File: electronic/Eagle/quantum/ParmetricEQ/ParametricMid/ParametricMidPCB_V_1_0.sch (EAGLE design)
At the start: 83 parts, among them IC1 OP275_SOIC8, IC14 TL072, IC2 OP275_SOIC8, IC3 OP275_SOIC8, IC4 DAC084S085CIMM_NOPB, IC5 DAC084S085CIMM_NOPB, J1 90814-0204, J2 90814-0204, Q1 TRANSOSTOR_NPN, Q2 TRANSOSTOR_NPN, U1 THAT2181SO8-US, U2 THAT2181SO8-US, U3 THAT2181SO8-US

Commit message: updates ParametricEQ
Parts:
- removed C19: 100 nF, passive components:CAPACITOR_0603
- removed C64: 10 uF, passive components:CAPACITOR_1206
- removed J1, J2: 90814-0204, electro_mechanical:90814-0204
- removed R60, R61, R67: 10 k, passive components:RESISTOR_0603
- removed R68: 20 k, passive components:RESISTOR_0603
- removed U$1, U$2: TL072, OP-AMPS:TL072
- removed Z1: ZENER_DIODE_BZT, passive components:ZENER_DIODE_BZT
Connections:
- removed net 1V_DAC_UNBUFFERD: C19.1, C64.1, R61.2, R68.1, U$2G$1.+IN
- removed net 2V_DAC_REF: R67.1, R68.2, Z1.K
- removed net AGND: C19.2, C64.2, R60.1, Z1.A
- removed net L-IN: J2.3
- removed net L-OUT: J2.4
- removed net N$67: R60.2, R61.1, U$2G$2.+IN
- net 0,5V_DAC: no longer U$2G$2.-IN, U$2G$2.OUT
- net 1V_DAC: no longer U$2G$1.-IN, U$2G$1.OUT
- net GND: no longer J1.3, J1.4
- net MID1_R-IN: no longer J2.1
- net MID1_R-OUT: no longer J2.2
- net V+: no longer J1.1, R67.2
- net V-: no longer J1.2
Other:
- note removed: "DAC Ref Voltages"

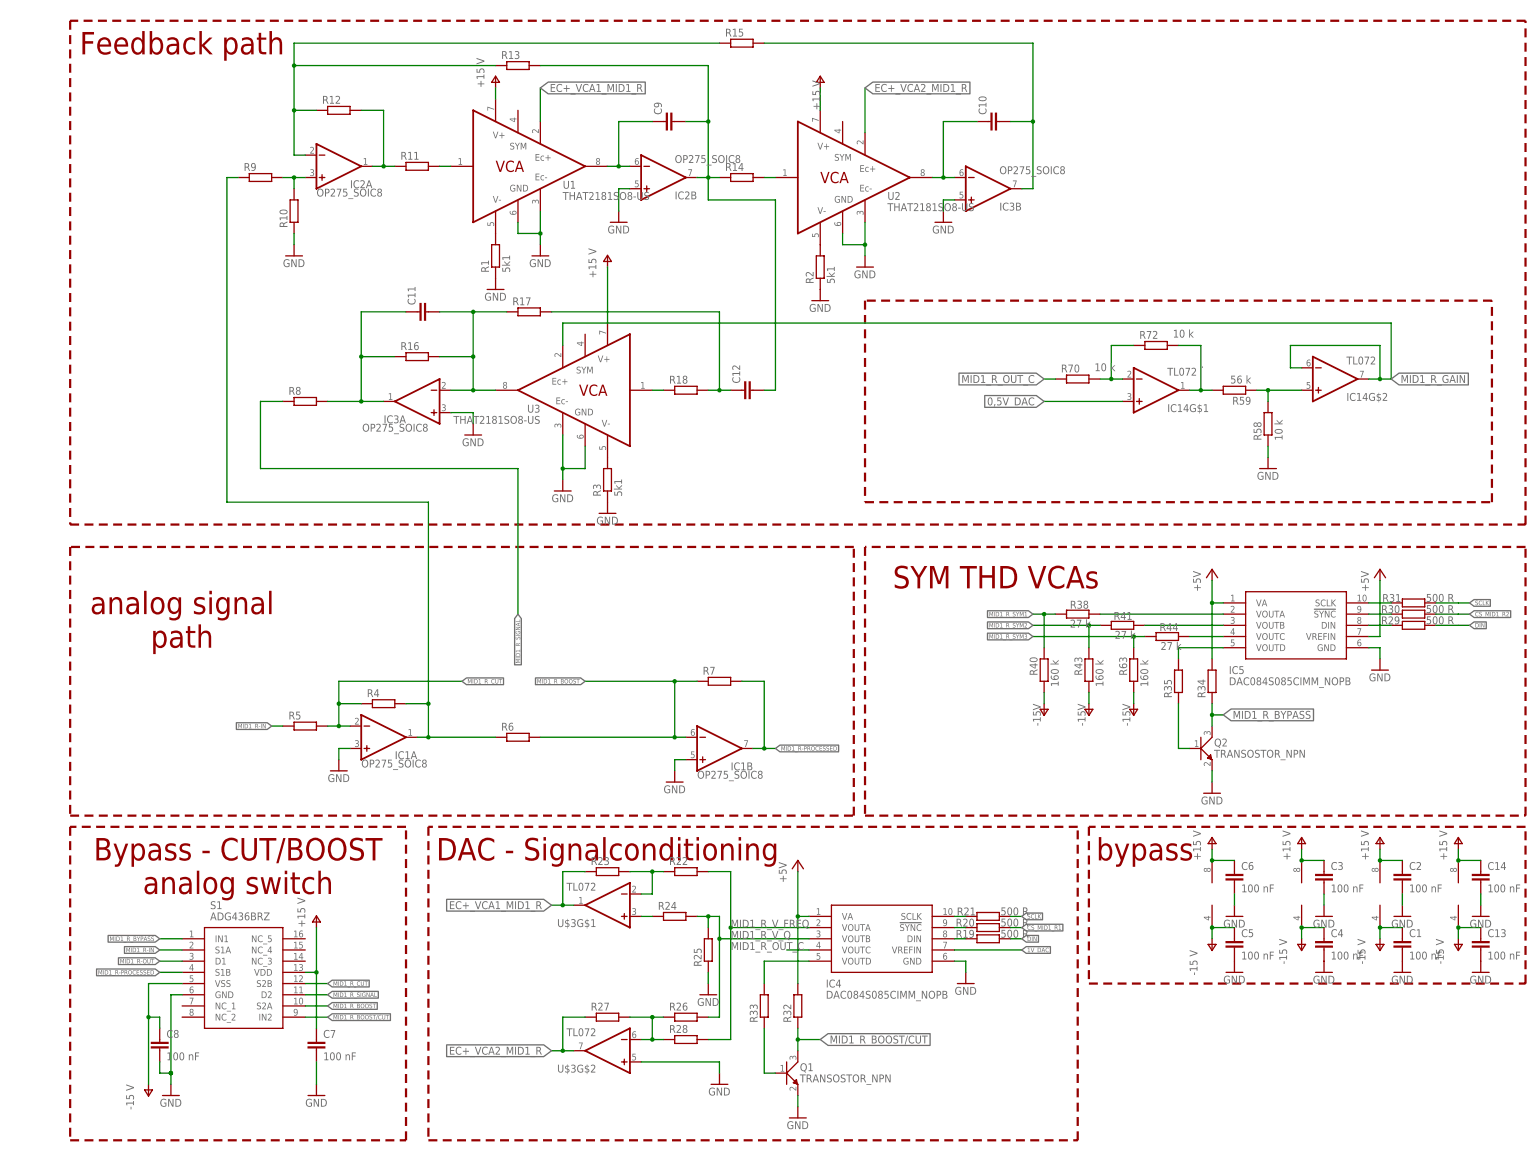
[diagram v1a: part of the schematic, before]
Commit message: split PCB in ParametricEQ
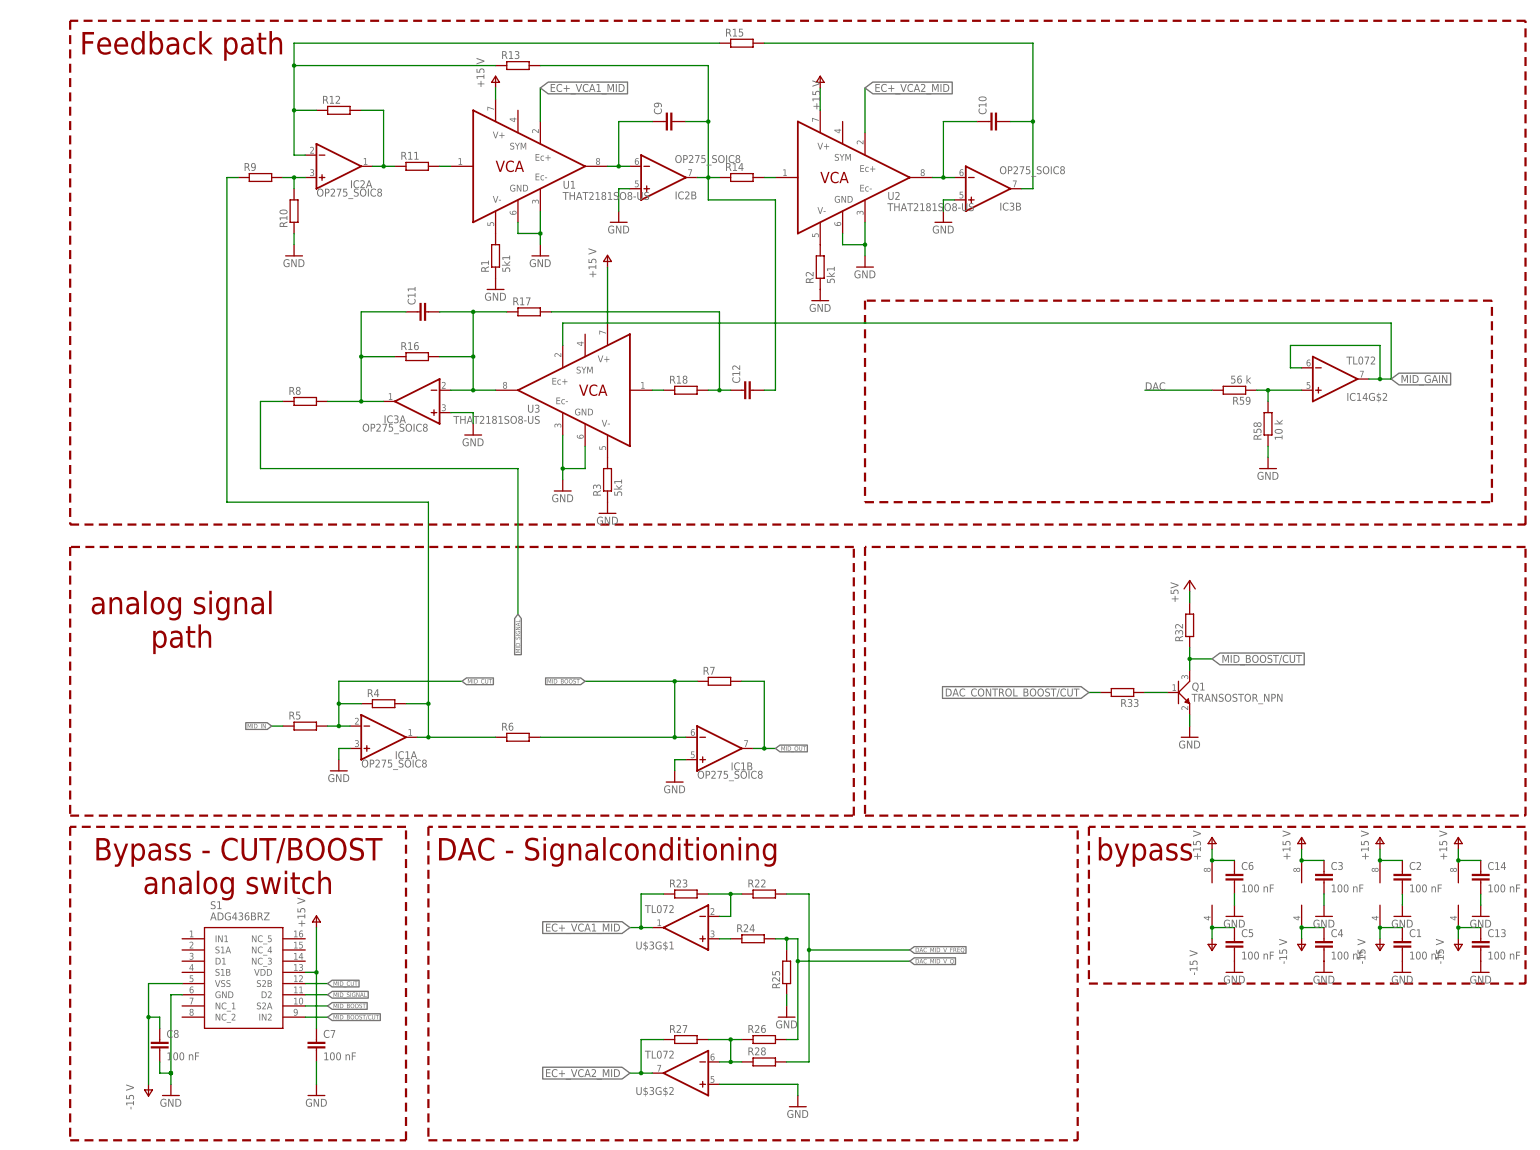
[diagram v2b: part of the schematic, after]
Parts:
- removed IC4, IC5: DAC084S085CIMM_NOPB, SPI:DAC084S085CIMM_NOPB
- removed Q2: TRANSOSTOR_NPN, active components:TRANSOSTOR_NPN
- removed R19, R20, R21, R29, R30, R31: 500 R, passive components:RESISTOR_0603
- removed R34, R35: (no value), passive components:RESISTOR_0603
- removed R38, R41, R44: 27 k, passive components:RESISTOR_0603
- removed R40, R43, R63: 160 k, passive components:RESISTOR_0603
- removed R70, R72: 10 k, passive components:RESISTOR_0603
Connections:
- net EC+_VCA1_MID1_R renamed EC+_VCA1_MID
- net EC+_VCA2_MID1_R renamed EC+_VCA2_MID
- net MID1_R_BOOST renamed MID_BOOST
- net MID1_R_BOOST/CUT renamed MID_BOOST/CUT
- net MID1_R_CUT renamed MID_CUT
- net MID1_R_GAIN renamed MID_GAIN
- net MID1_R_SIGNAL renamed MID_SIGNAL
- removed net .: IC14G$1.OUT, R59.2, R72.2
- removed net 0,5V_DAC: IC14G$1.+IN
- removed net 1V_DAC: IC4.VREFIN
- removed net CS_MID1_R1: R20.2, R30.2
- removed net DIN: R19.2
- removed net DIN1: R29.2
- removed net MID1_R-IN: R5.1, S1.S1A
- removed net MID1_R-OUT: S1.D1
- removed net MID1_R-PROCESSED: IC1B.OUT, R7.2, S1.S1B
- removed net MID1_R_BYPASS: Q2.C, R34.1, S1.IN1
- removed net MID1_R_OUT_C: IC4.VOUTC, R70.1
- removed net MID1_R_SYM1: R38.1, R40.2
- removed net MID1_R_SYM2: R41.1, R43.2
- removed net MID1_R_SYM3: R44.1, R63.2
- removed net MID1_R_V_FREQ: IC4.VOUTA, R22.2, R28.2
- removed net MID1_R_V_Q: IC4.VOUTB, R24.2, R25.2, R26.2
- removed net N$18: IC4.DIN, R19.1
- removed net N$19: IC4.!SYNC, R20.1
- removed net N$20: IC4.SCLK, R21.1
- removed net N$24: IC5.DIN, R29.1
- removed net N$25: IC5.!SYNC, R30.1
- removed net N$26: IC4.VOUTD, R33.2
- removed net N$27: IC5.SCLK, R31.1
- removed net N$28: Q2.B, R35.1
- removed net N$30: IC5.VOUTD, R35.2
- removed net N$56: IC5.VOUTA, R38.2
- removed net N$57: IC5.VOUTB, R41.2
- removed net N$58: IC5.VOUTC, R44.2
- removed net N$74: IC14G$1.-IN, R70.2, R72.1
- removed net SCLK: R21.2
- removed net SCLK1: R31.2
- new net DAC: R59.2
- new net DAC_CONTROL_BOOST/CUT: R33.2
- new net DAC_MID_V_FREQ: R22.2, R28.2
- new net DAC_MID_V_Q: R24.2, R25.2, R26.2
- new net MID_IN: R5.1
- new net MID_OUT: IC1B.OUT, R7.2
- net +5V: no longer IC4.VA, IC5.VA, IC5.VREFIN, R34.2
- net GND: no longer IC4.GND, IC5.GND, Q2.E
- net V-: no longer R40.1, R43.1, R63.1
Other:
- note removed: "SYM THD VCAs"
- moved on the sheet: Q1, R22, R23, R24, R25, R26, R27, R28, R32, R33, U$3G$1, U$3G$2
